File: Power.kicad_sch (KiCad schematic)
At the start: 68 parts, among them J1 DBT50G-9.5-2P, J2 DBT50G-9.5-2P, J3 DBT50G-9.5-2P, J38 2.54-1*4, J4 DBT50G-9.5-2P, U3 TPS552872, U4 TPS62A02A

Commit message: Rename 12V nets to VIN_SYS/VZ1-VZ4, update README for v5
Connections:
- net +12V_SYS renamed VIN_SYS
- net +12V_Z1 renamed VZ1
- net +12V_Z2 renamed VZ2
- net +12V_Z3 renamed VZ3
- net +12V_Z4 renamed VZ4
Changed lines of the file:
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@@
 			)
 		)
-		(property "Value" "+12V_Z2"
+		(property "Value" "VZ2"
 			(at 256.54 122.555 0)
 			(show_name no)
@@
 			)
 		)
-		(property "Value" "+12V_Z3"
+		(property "Value" "VZ3"
 			(at 180.34 139.7 0)
 			(show_name no)
@@
 			)
 		)
-		(property "Value" "+12V_Z4"
+		(property "Value" "VZ4"
 			(at 269.494 145.542 0)
 			(show_name no)
@@
 			)
 		)
-		(property "Value" "+12V_Z4"
+		(property "Value" "VZ4"
 			(at 184.15 127 0)
 			(show_name no)
@@
 			)
 		)
-		(property "Value" "+12V_Z2"
+		(property "Value" "VZ2"
 			(at 167.64 139.7 0)
 			(show_name no)
@@
 			)
 		)
-		(property "Value" "+12V_SYS"
+		(property "Value" "VIN_SYS"
 			(at 234.95 48.26 0)
 			(show_name no)
@@
 			)
 		)
-		(property "Value" "+12V_Z1"
+		(property "Value" "VZ1"
 			(at 181.61 89.662 0)
 			(show_name no)
@@
 			)
 		)
-		(property "Value" "+12V_SYS"
+		(property "Value" "VIN_SYS"
 			(at 27.94 74.93 0)
 			(show_name no)
@@
 			)
 		)
-		(property "Value" "+12V_SYS"
+		(property "Value" "VIN_SYS"
 			(at 22.86 41.91 0)
 			(show_name no)
@@
 			)
 		)
-		(property "Value" "+12V_SYS"
+		(property "Value" "VIN_SYS"
 			(at 60.96 54.61 0)
 			(show_name no)
@@
 			)
 		)
-		(property "Value" "+12V_Z1"
+		(property "Value" "VZ1"
 			(at 240.792 146.05 0)
 			(show_name no)
@@
 			)
 		)
-		(property "Value" "+12V_SYS"
+		(property "Value" "VIN_SYS"
 			(at 234.95 150.876 0)
 			(show_name no)
@@
 			)
 		)
-		(property "Value" "+12V_Z4"
+		(property "Value" "VZ4"
 			(at 276.86 122.555 0)
 			(show_name no)
@@
 			)
 		)
-		(property "Value" "+12V_Z3"
+		(property "Value" "VZ3"
 			(at 184.15 114.3 0)
 			(show_name no)
@@
 			)
 		)
-		(property "Value" "+12V_Z1"
+		(property "Value" "VZ1"
 			(at 154.94 139.7 0)
 			(show_name no)
@@
 			)
 		)
-		(property "Value" "+12V_Z2"
+		(property "Value" "VZ2"
 			(at 184.15 101.6 0)
 			(show_name no)
@@
 			)
 		)
-		(property "Value" "+12V_Z2"
+		(property "Value" "VZ2"
 			(at 251.206 145.796 0)
 			(show_name no)
@@
 			)
 		)
-		(property "Value" "+12V_Z1"
+		(property "Value" "VZ1"
 			(at 246.38 122.555 0)
 			(show_name no)
@@
 			)
 		)
-		(property "Value" "+12V_Z3"
+		(property "Value" "VZ3"
 			(at 260.35 145.796 0)
 			(show_name no)
@@
 			)
 		)
-		(property "Value" "+12V_Z3"
+		(property "Value" "VZ3"
 			(at 266.7 122.555 0)
 			(show_name no)
@@
 			)
 		)
-		(property "Value" "+12V_Z4"
+		(property "Value" "VZ4"
 			(at 193.04 139.7 0)
 			(show_name no)

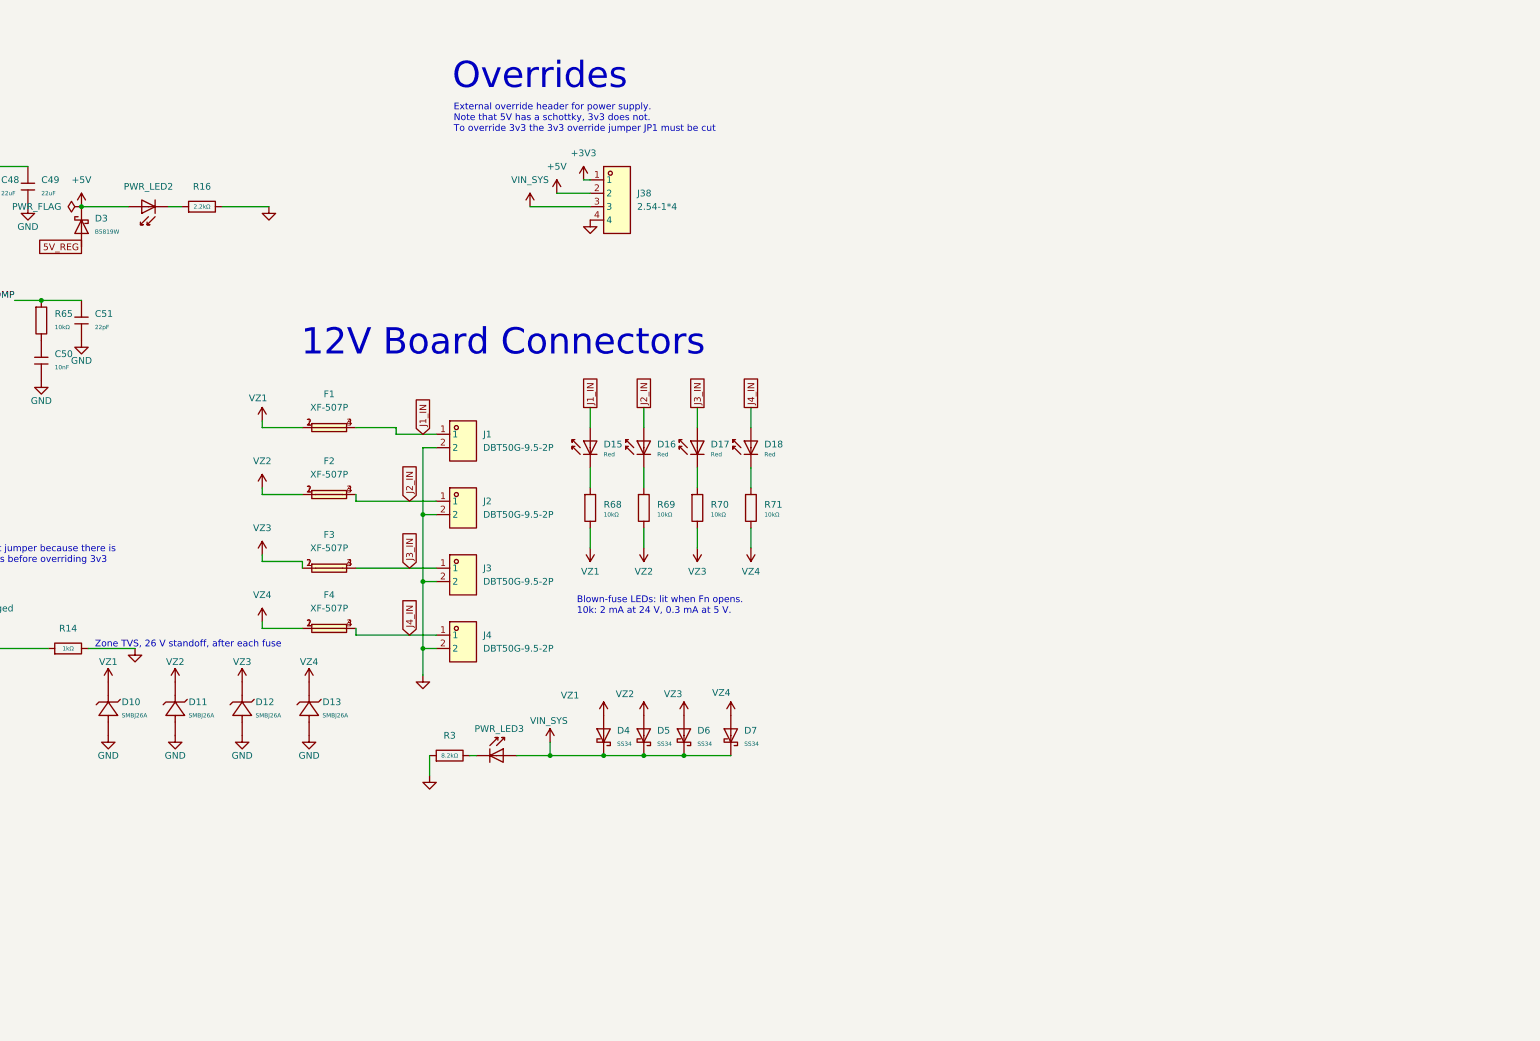
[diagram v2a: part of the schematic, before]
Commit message: Ideal diode per zone input: LM74700 + BSC014N06NS after each fuse
Reverse-polarity protection for all four zone inputs. Each fuse output is a
new net Zn_F; an LM74700QDBVTQ1 (U11-U14) drives an Infineon BSC014N06NS
(Q1-Q4, 60 V, 1.45 mOhm, C113391) from Zn_F to VZn, with 100 nF for VCAP,
input and output (C54-C65). The zone TVS and OR diodes stay on VZn; the
blown-fuse LEDs read across the fuse only.

Board: FETs west of each fuse's output pins with Zn_F and VZn pours, drain
stitched to the B.Cu VZ band, EN via In2. TVS D10-D13 moved, zone 1 VIN_SYS
hops on In2 along x 225, zone 4 VIN_SYS moved to y 39.85. FET 3D model
offset fixed to sit on its pads. Power sheet now A3.
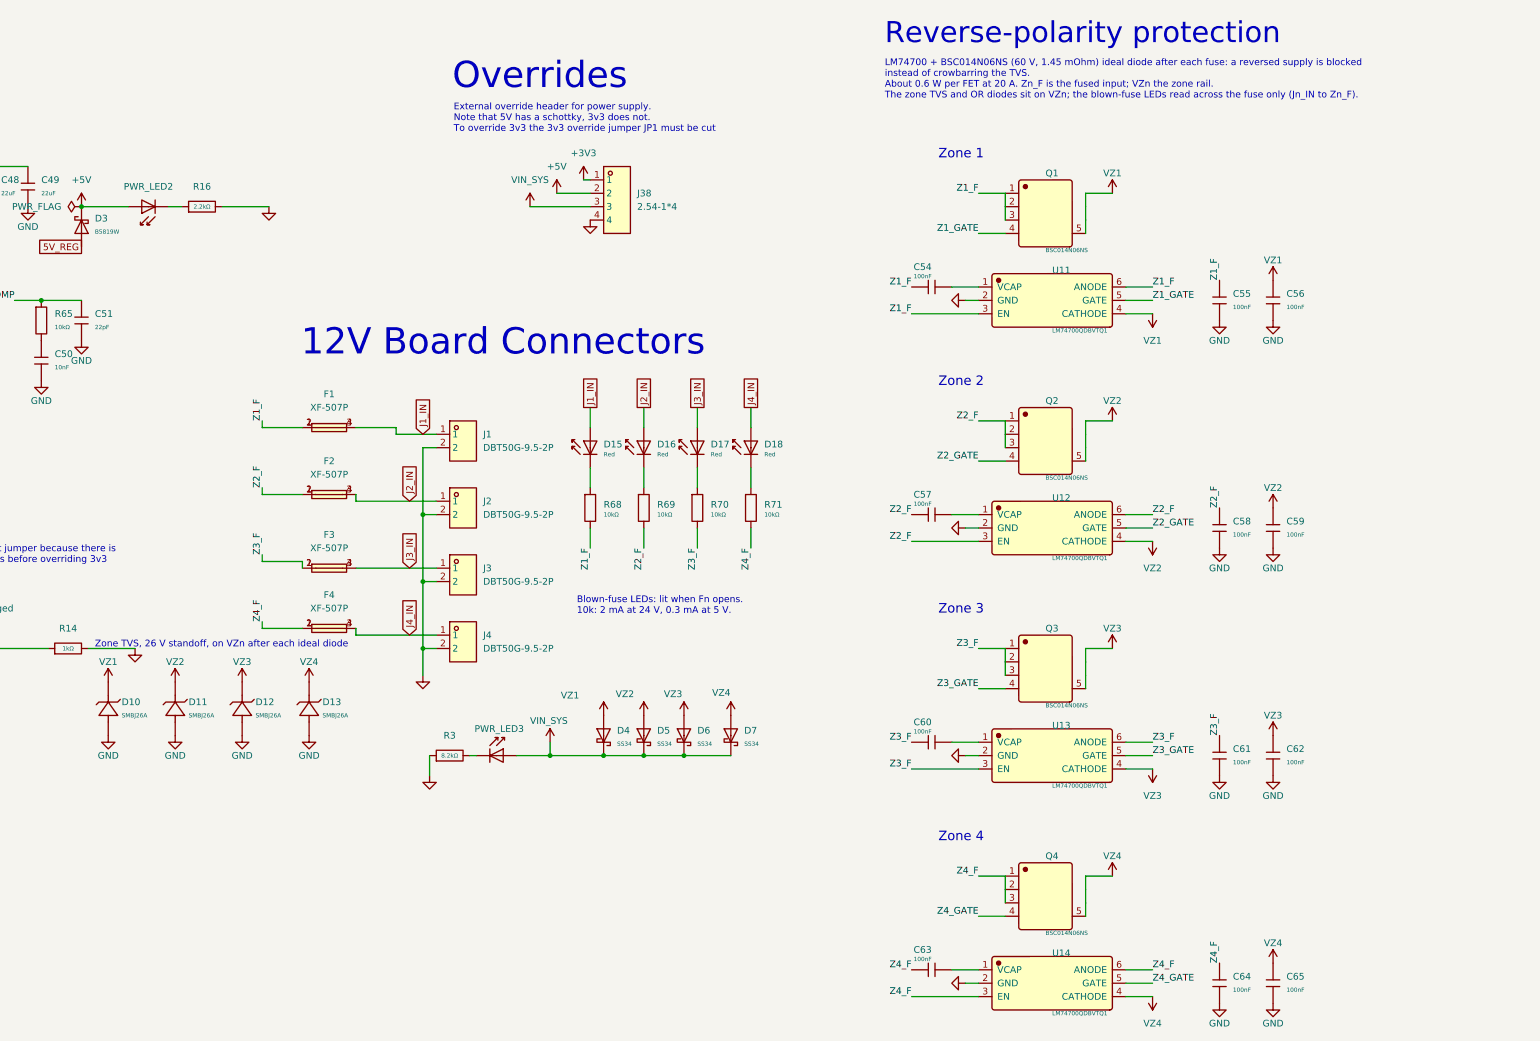
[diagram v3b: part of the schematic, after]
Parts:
- added C54, C55, C56, C57, C58, C59, C60, C61, C62, C63, C64, C65: 100nF, PixelBlit:C_0603, symbol PixelBlit:0603,100nF
- added Q1, Q2, Q3, Q4: BSC014N06NS, JLCImport:BSC014N06NS, symbol JLCImport:BSC014N06NS
- added U11, U12, U13, U14: LM74700QDBVTQ1, JLCImport:LM74700QDBVTQ1, symbol JLCImport:LM74700QDBVTQ1
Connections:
- net GND: now also C55.2, C56.2, C58.2, C59.2, C61.2, C62.2, C64.2, C65.2, U11.2 (GND), U12.2 (GND), U13.2 (GND), U14.2 (GND)
- net VZ1: now also C56.1, Q1.5 (D), U11.4 (CATHODE); no longer F1.1, F1.2, R68.2
- net VZ2: now also C59.1, Q2.5 (D), U12.4 (CATHODE); no longer F2.1, F2.2, R69.2
- net VZ3: now also C62.1, Q3.5 (D), U13.4 (CATHODE); no longer F3.1, F3.2, R70.2
- net VZ4: now also C65.1, Q4.5 (D), U14.4 (CATHODE); no longer F4.1, F4.2, R71.2
- new net: C60.2, U13.1 (VCAP)
- new net: C57.2, U12.1 (VCAP)
- new net: C63.2, U14.1 (VCAP)
- new net: C54.2, U11.1 (VCAP)
- new net Z1_F: C54.1, C55.1, F1.1, F1.2, Q1.1 (S), Q1.2 (S), Q1.3 (S), R68.2, U11.3 (EN), U11.6 (ANODE)
- new net Z1_GATE: Q1.4 (G), U11.5 (GATE)
- new net Z2_F: C57.1, C58.1, F2.1, F2.2, Q2.1 (S), Q2.2 (S), Q2.3 (S), R69.2, U12.3 (EN), U12.6 (ANODE)
- new net Z2_GATE: Q2.4 (G), U12.5 (GATE)
- new net Z3_F: C60.1, C61.1, F3.1, F3.2, Q3.1 (S), Q3.2 (S), Q3.3 (S), R70.2, U13.3 (EN), U13.6 (ANODE)
- new net Z3_GATE: Q3.4 (G), U13.5 (GATE)
- new net Z4_F: C63.1, C64.1, F4.1, F4.2, Q4.1 (S), Q4.2 (S), Q4.3 (S), R71.2, U14.3 (EN), U14.6 (ANODE)
- new net Z4_GATE: Q4.4 (G), U14.5 (GATE)
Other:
- note added: "LM74700 + BSC014N06NS (60 V, 1.45 mOhm) ideal diode after each fuse: a reversed supply is blocked instead of crowbarring the TVS. About 0.6 W per FET at 20 A. Zn_F is the fused input; VZn the zone rail. The zone TVS and OR diodes sit on VZn; the blown-fuse LEDs read across the fuse only (Jn_IN to Zn_F)."
- note added: "Reverse-polarity protection"
- note added: "Zone 1"
- note added: "Zone 2"
- note added: "Zone 3"
- note added: "Zone 4"
- note added: "Zone TVS, 26 V standoff, on VZn after each ideal diode"
- note removed: "Zone TVS, 26 V standoff, after each fuse"
